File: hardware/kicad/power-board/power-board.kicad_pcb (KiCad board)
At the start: 4 copper layers, 120 x 90 mm, 14 parts, among them J1 3.3V LoRaWAN, J2 3.3V SWARM, J4 5V, J6 12V

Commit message: initial test board
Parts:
- added G***: LOGO, Teapot:TeapotLogo, F.Cu at (190.0, 83.5)
- added G***: LOGO, Teapot:TeapotLogo, B.Cu at (112.0, 119.5)
- added J3: Conn_01x02, Teapot:Makeit_USB_C_PD_Trigger, B.Cu at (101.0, 97.0)
- added U1: 3V3, Teapot:LM2596Module, B.Cu at (172.7, 106.2)
- added U2: 3V3, Teapot:LM2596Module, B.Cu at (132.3, 117.2)
- added U3: 5V, Teapot:LM2596Module, B.Cu at (151.8, 77.4)
- added U4: 3V3, Teapot:MiniMP1584ENModule, F.Cu at (172.7, 105.2)
- added U5: 3V3, Teapot:MiniMP1584ENModule, F.Cu at (133.3, 116.8)
- added U6: 5V, Teapot:MiniMP1584ENModule, F.Cu at (151.1, 76.2)
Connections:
- J1 pad 1: GND -> /+3.3vL
- J1 pad 2: /+3.3vL -> GND
- J4 pad 1: GND -> /+5v
- J4 pad 2: /+5v -> GND
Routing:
- net /+12v: track 0.00 -> 185.8 mm
- net /+5v: track 0.00 -> 76.8 mm
- net /+3.3vL: track 0.00 -> 72.8 mm
- net /+3.3vS: track 0.00 -> 42.9 mm
- net GND: vias 0 -> 113
- removed copper zone on In1.Cu, net GND
- removed copper zone on In2.Cu, net GND
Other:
- copper layers 4 -> 2
- board text added: "12V"
- board text added: "3V3"
- board text added: "5V"
- board text added: "INPUT"
- board text added: "OUTPUT"
- board text added: "Power Board"
- board text added: "Revision 1 (Test Board)"
- board text added: "Teapot BWSL1A"
- board text added: "Test board to power Teapot BWSL1A"

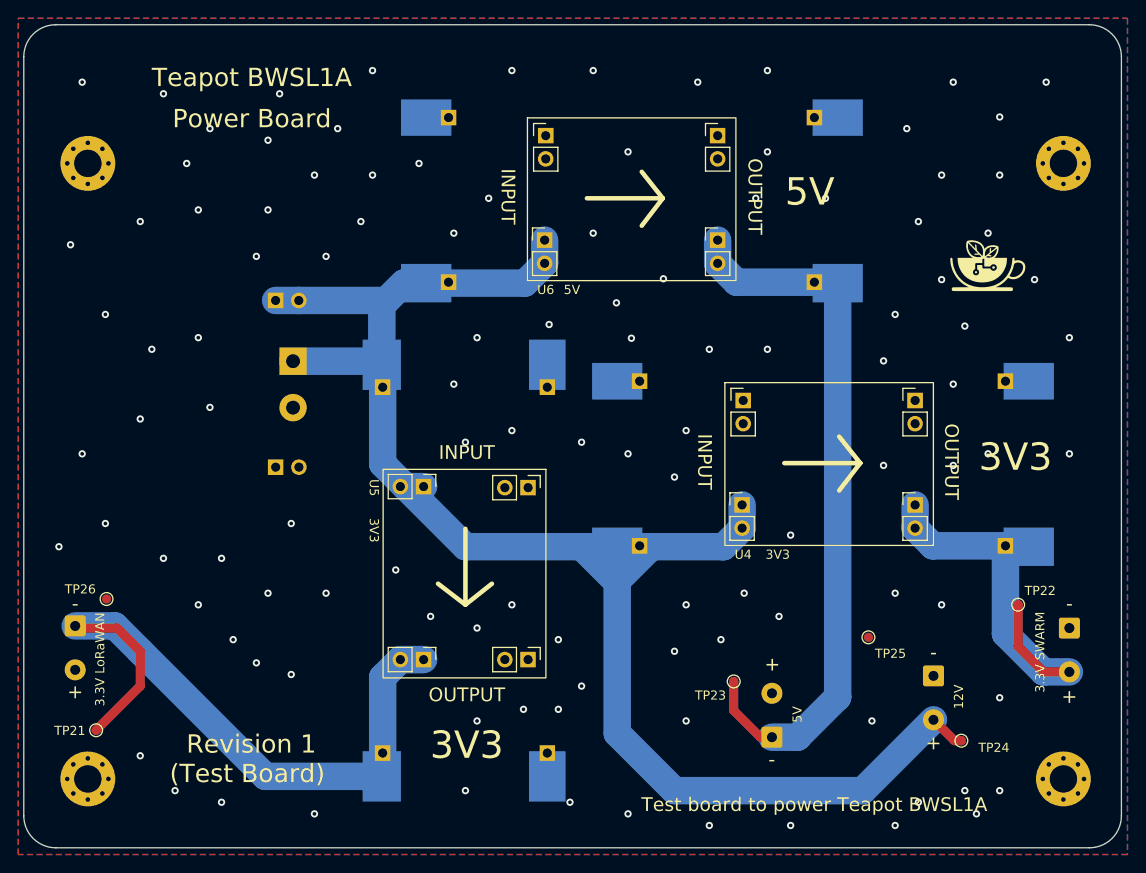
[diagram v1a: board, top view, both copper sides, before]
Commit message: fix power polarity in power board test
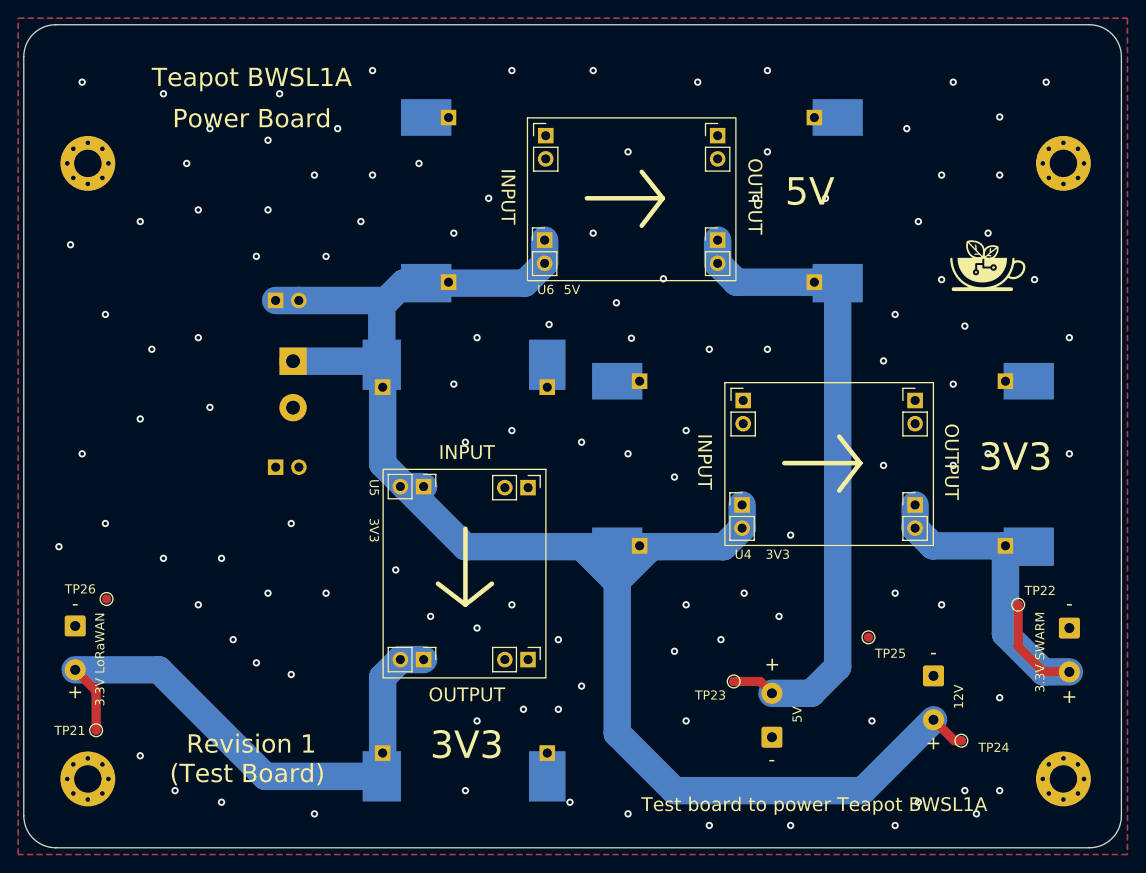
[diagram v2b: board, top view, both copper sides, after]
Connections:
- J1 pad 1: /+3.3vL -> GND
- J1 pad 2: GND -> /+3.3vL
- J4 pad 1: /+5v -> GND
- J4 pad 2: GND -> /+5v
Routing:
- net /+3.3vL: track 72.8 -> 59.5 mm
- net /+5v: track 76.8 -> 69.0 mm
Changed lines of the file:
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@@
     (fp_circle (center 4.8 0) (end 5.95 0) (layer "F.Fab") (width 0.1) (fill none))
     (pad "1" thru_hole roundrect locked (at 0 0 270) (size 2.3 2.3) (drill 1.1) (layers *.Cu *.Mask) (roundrect_rratio 0.108696087)
-      (net 3 "/+3.3vL") (pinfunction "Pin_1") (pintype "passive"))
+      (net 1 "GND") (pinfunction "Pin_1") (pintype "passive"))
     (pad "2" thru_hole circle locked (at 4.8 0 270) (size 2.3 2.3) (drill 1.1) (layers *.Cu *.Mask)
-      (net 1 "GND") (pinfunction "Pin_2") (pintype "passive"))
+      (net 3 "/+3.3vL") (pinfunction "Pin_2") (pintype "passive"))
     (model "${KICAD6_3DMODEL_DIR}/Connector_Wire.3dshapes/SolderWire-0.5sqmm_1x02_P4.8mm_D0.9mm_OD2.3mm.wrl"
       (offset (xyz 0 0 0))
@@
     (fp_circle (center 4.8 0) (end 5.95 0) (layer "F.Fab") (width 0.1) (fill none))
     (pad "1" thru_hole roundrect locked (at 0 0 90) (size 2.3 2.3) (drill 1.1) (layers *.Cu *.Mask) (roundrect_rratio 0.108696087)
-      (net 2 "/+5v") (pinfunction "Pin_1") (pintype "passive"))
+      (net 1 "GND") (pinfunction "Pin_1") (pintype "passive"))
     (pad "2" thru_hole circle locked (at 4.8 0 90) (size 2.3 2.3) (drill 1.1) (layers *.Cu *.Mask)
-      (net 1 "GND") (pinfunction "Pin_2") (pintype "passive"))
+      (net 2 "/+5v") (pinfunction "Pin_2") (pintype "passive"))
     (model "${KICAD6_3DMODEL_DIR}/Connector_Wire.3dshapes/SolderWire-0.5sqmm_1x02_P4.8mm_D0.9mm_OD2.3mm.wrl"
       (offset (xyz 0 0 0))
@@
     )
     (fp_poly (pts
+        (xy 1.173396 -0.140034)
+        (xy 1.218303 -0.182414)
+        (xy 1.242867 -0.241853)
+        (xy 1.245421 -0.270461)
+        (xy 1.230771 -0.32823)
+        (xy 1.19246 -0.374836)
+        (xy 1.13895 -0.404832)
+        (xy 1.078703 -0.412773)
+        (xy 1.039171 -0.403207)
+        (xy 0.988625 -0.366812)
+        (xy 0.960372 -0.315237)
+        (xy 0.954064 -0.256796)
+        (xy 0.969351 -0.199801)
+        (xy 1.005887 -0.152565)
+        (xy 1.050737 -0.127193)
+        (xy 1.115191 -0.119898)
+      ) (layer "B.SilkS") (width 0) (fill solid))
+    (fp_poly (pts
         (xy -1.11108 2.702231)
         (xy -0.926392 2.674056)
@@
       ) (layer "B.SilkS") (width 0) (fill solid))
     (fp_poly (pts
-        (xy 1.173396 -0.140034)
-        (xy 1.218303 -0.182414)
-        (xy 1.242867 -0.241853)
-        (xy 1.245421 -0.270461)
-        (xy 1.230771 -0.32823)
-        (xy 1.19246 -0.374836)
-        (xy 1.13895 -0.404832)
-        (xy 1.078703 -0.412773)
-        (xy 1.039171 -0.403207)
-        (xy 0.988625 -0.366812)
-        (xy 0.960372 -0.315237)
-        (xy 0.954064 -0.256796)
-        (xy 0.969351 -0.199801)
-        (xy 1.005887 -0.152565)
-        (xy 1.050737 -0.127193)
-        (xy 1.115191 -0.119898)
-      ) (layer "B.SilkS") (width 0) (fill solid))
-    (fp_poly (pts
-        (xy -0.76013 -0.675219)
-        (xy -0.728503 -0.696094)
-        (xy -0.70202 -0.743142)
-        (xy -0.695876 -0.785817)
-        (xy -0.707628 -0.843914)
-        (xy -0.728503 -0.875541)
-        (xy -0.775551 -0.902024)
-        (xy -0.818227 -0.908168)
-        (xy -0.876323 -0.896416)
-        (xy -0.90795 -0.875541)
-        (xy -0.934433 -0.828493)
-        (xy -0.940577 -0.785817)
-        (xy -0.928825 -0.727721)
-        (xy -0.90795 -0.696094)
-        (xy -0.860902 -0.669611)
-        (xy -0.818227 -0.663467)
-      ) (layer "B.SilkS") (width 0) (fill solid))
-    (fp_poly (pts
         (xy 3.311113 0.796783)
         (xy 3.358751 0.764699)
@@
         (xy 3.255826 0.800877)
       ) (layer "B.SilkS") (width 0) (fill solid))
+    (fp_poly (pts
+        (xy -0.76013 -0.675219)
+        (xy -0.728503 -0.696094)
+        (xy -0.70202 -0.743142)
+        (xy -0.695876 -0.785817)
+        (xy -0.707628 -0.843914)
+        (xy -0.728503 -0.875541)
+        (xy -0.775551 -0.902024)
+        (xy -0.818227 -0.908168)
+        (xy -0.876323 -0.896416)
+        (xy -0.90795 -0.875541)
+        (xy -0.934433 -0.828493)
+        (xy -0.940577 -0.785817)
+        (xy -0.928825 -0.727721)
+        (xy -0.90795 -0.696094)
+        (xy -0.860902 -0.669611)
+        (xy -0.818227 -0.663467)
+      ) (layer "B.SilkS") (width 0) (fill solid))
   )
   (footprint "Teapot:LM2596Module" (layer "B.Cu")
@@
     (effects (font (size 1.5 1.5) (thickness 0.3)))
   )
+  (segment (start 90.906 123.19) (end 90.678 122.962) (width 1) (layer "F.Cu") (net 1))
   (via (at 146.05 129.54) (size 0.8) (drill 0.4) (layers "F.Cu" "B.Cu") (free) (net 1))
   (via (at 186.69 63.5) (size 0.8) (drill 0.4) (layers "F.Cu" "B.Cu") (free) (net 1))
@@
   (via (at 165.1 76.2) (size 0.8) (drill 0.4) (layers "F.Cu" "B.Cu") (free) (net 1))
   (via (at 144.78 142.24) (size 0.8) (drill 0.4) (layers "F.Cu" "B.Cu") (free) (net 1))
-  (segment (start 162.687 132.207) (end 165.607 135.127) (width 1) (layer "F.Cu") (net 2))
-  (segment (start 165.607 135.127) (end 166.867 135.127) (width 1) (layer "F.Cu") (net 2))
-  (segment (start 162.687 129.032) (end 162.687 132.207) (width 1) (layer "F.Cu") (net 2))
+  (segment (start 162.687 129.032) (end 165.572 129.032) (width 1) (layer "F.Cu") (net 2))
+  (segment (start 165.572 129.032) (end 166.867 130.327) (width 1) (layer "F.Cu") (net 2))
   (segment (start 160.93 83.312) (end 160.93 80.772) (width 3) (layer "B.Cu") (net 2))
-  (segment (start 169.673 135.127) (end 166.867 135.127) (width 3) (layer "B.Cu") (net 2))
+  (segment (start 174.056 85.472) (end 174.056 127.442) (width 3) (layer "B.Cu") (net 2))
   (segment (start 171.506 85.372) (end 162.99 85.372) (width 3) (layer "B.Cu") (net 2))
-  (segment (start 174.056 85.472) (end 174.056 130.744) (width 3) (layer "B.Cu") (net 2))
+  (segment (start 171.171 130.327) (end 166.867 130.327) (width 3) (layer "B.Cu") (net 2))
   (segment (start 162.99 85.372) (end 160.93 83.312) (width 3) (layer "B.Cu") (net 2))
-  (segment (start 174.056 130.744) (end 169.673 135.127) (width 3) (layer "B.Cu") (net 2))
-  (segment (start 97.155 125.095) (end 96.52 124.46) (width 1) (layer "F.Cu") (net 3))
-  (segment (start 95.885 123.825) (end 95.25 123.19) (width 1) (layer "F.Cu") (net 3))
-  (segment (start 90.906 123.19) (end 90.678 122.962) (width 1) (layer "F.Cu") (net 3))
-  (segment (start 92.964 134.366) (end 97.79 129.54) (width 1) (layer "F.Cu") (net 3))
-  (segment (start 97.79 125.73) (end 97.155 125.095) (width 1) (layer "F.Cu") (net 3))
-  (segment (start 95.25 123.19) (end 90.906 123.19) (width 1) (layer "F.Cu") (net 3))
-  (segment (start 96.52 124.46) (end 95.885 123.825) (width 1) (layer "F.Cu") (net 3))
-  (segment (start 97.79 129.54) (end 97.79 125.73) (width 1) (layer "F.Cu") (net 3))
+  (segment (start 174.056 127.442) (end 171.171 130.327) (width 3) (layer "B.Cu") (net 2))
+  (segment (start 92.964 130.048) (end 90.678 127.762) (width 1) (layer "F.Cu") (net 3))
+  (segment (start 92.964 134.366) (end 92.964 130.048) (width 1) (layer "F.Cu") (net 3))
+  (segment (start 111.468 139.408) (end 99.822 127.762) (width 3) (layer "B.Cu") (net 3))
   (segment (start 124.3 128.578) (end 126.238 126.64) (width 3) (layer "B.Cu") (net 3))
   (segment (start 124.3 136.858) (end 124.3 128.578) (width 3) (layer "B.Cu") (net 3))
-  (segment (start 97.79 125.73) (end 111.468 139.408) (width 3) (layer "B.Cu") (net 3))
   (segment (start 111.468 139.408) (end 124.2 139.408) (width 3) (layer "B.Cu") (net 3))
-  (segment (start 90.678 122.962) (end 95.022 122.962) (width 3) (layer "B.Cu") (net 3))
+  (segment (start 99.822 127.762) (end 90.678 127.762) (width 3) (layer "B.Cu") (net 3))
   (segment (start 126.238 126.64) (end 128.778 126.64) (width 3) (layer "B.Cu") (net 3))
-  (segment (start 95.022 122.962) (end 97.79 125.73) (width 3) (layer "B.Cu") (net 3))
   (segment (start 196.57 127.99) (end 199.39 127.99) (width 1) (layer "F.Cu") (net 4))
   (segment (start 193.787 125.207) (end 196.57 127.99) (width 1) (layer "F.Cu") (net 4))
